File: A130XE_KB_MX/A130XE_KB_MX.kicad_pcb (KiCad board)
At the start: 2 copper layers, 330 x 131 mm, 76 parts, among them J1 34 pin RIBBON KEYBOARD CABLE, J2 Conn_01x02_Male, SW1 KS_RESET, SW10 K_5, SW11 K_I, SW12 K_T, SW13 K_G, SW14 K_SPACE, SW15 K_B, SW16 K_K, SW17 KS_SELECT, SW18 K_4, SW19 K_O, SW2 K_6, SW20 K_R, SW21 K_F, SW22 K_M, SW23 K_V, SW24 K_L, SW25 K_3, SW26 K_P, SW27 K_E, SW28 K_D, SW29 KS_START, SW3 K_U, SW30 K_comma, SW31 K_comdot, SW32 K_C, SW33 K_dot, SW34 K_2, SW35 K_minus, SW36 K_W, SW37 K_S, SW38 K_X, SW39 K_plus, SW4 K_Y, SW40 K_1, SW41 K_equal, SW42 K_Q, SW43 K_A, SW44 K_slash, SW45 K_asterisk, SW46 K_Z, SW47 K_ATARI, SW48 K_ESC, SW49 K_RETURN, SW5 K_H, SW50 K_TAB, SW51 K_CAPS, SW52 K_CTRL, SW53 K_LSHIFT, SW54 K_RSHIFT, SW55 K_BRK, SW56 K_DEL, SW57 K_GT, SW58 K_LT, SW59 K_0, SW6 K_N, SW60 K_9, SW61 K_8, SW62 K_7, SW63 K_SPACE_1, SW64 K_SPACE_2, SW65 K_F1, SW66 K_F2, SW67 K_F3, SW68 K_F4, SW7 KS_HELP, SW8 K_J, SW9 KS_OPTION

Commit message: New layout for spacebar 6.25 and two 1.25 at side. Function keys are 1.5u.
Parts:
- moved SW63 7.15 mm to (141.5, 198.1)
- moved SW64 2.41 mm to (284.3, 198.1)
- moved SW14 2.37 mm to (212.9, 198.1)
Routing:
- net OUT_7: track 413.6 -> 373.7 mm, vias 0 -> 1
- net IN_2: track 260.2 -> 297.0 mm
- net RSC: track 436.5 -> 402.2 mm, vias 2 -> 3
- net OUT_5: track 512.3 -> 480.4 mm, vias 1 -> 2
- net SELECT: track 178.8 -> 150.8 mm, vias 2 -> 0
- net GND: track 483.9 -> 457.2 mm, vias 0 -> 1
- net IN_5: track 304.5 -> 326.2 mm, vias 1 -> 0
- net IN_7: track 295.3 -> 316.0 mm, vias 2 -> 5
- net OPTION: track 124.9 -> 143.1 mm, vias 0 -> 1
- net START: track 163.6 -> 148.8 mm
- net IN_1: track 336.4 -> 325.1 mm, vias 1 -> 0
- net IN_6: track 314.3 -> 304.2 mm, vias 2 -> 0
- net IN_0: track 390.9 -> 400.5 mm, vias 4 -> 1
- net IN_4: track 356.1 -> 349.5 mm, vias 1 -> 0
- net OUT_4: track 287.7 -> 281.6 mm
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- added copper zone on B.Cu, net GND
- removed copper zone on B.Cu, net +5V

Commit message: Changed layout of buttons surrounding the spacebar. Atari XE seems to have 9U spacebar, so we are using 6.25u (more common) and two keys around it (1.25u and 1.50u)
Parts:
- SW63: footprint Button_Switch_Keyboard:SW_Cherry_MX1A_1.00u_PCB -> Button_Switch_Keyboard:SW_Cherry_MX1A_1.25u_PCB
- SW64: footprint Button_Switch_Keyboard:SW_Cherry_MX1A_1.00u_PCB -> Button_Switch_Keyboard:SW_Cherry_MX1A_1.50u_PCB
- moved SW64 2.41 mm to (286.8, 198.1)
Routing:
- net Net-(J2-Pad1): track 170.3 -> 174.8 mm, vias 0 -> 2
- net GND: track 457.2 -> 461.5 mm
- net IN_6: track 304.2 -> 302.9 mm, vias 0 -> 1

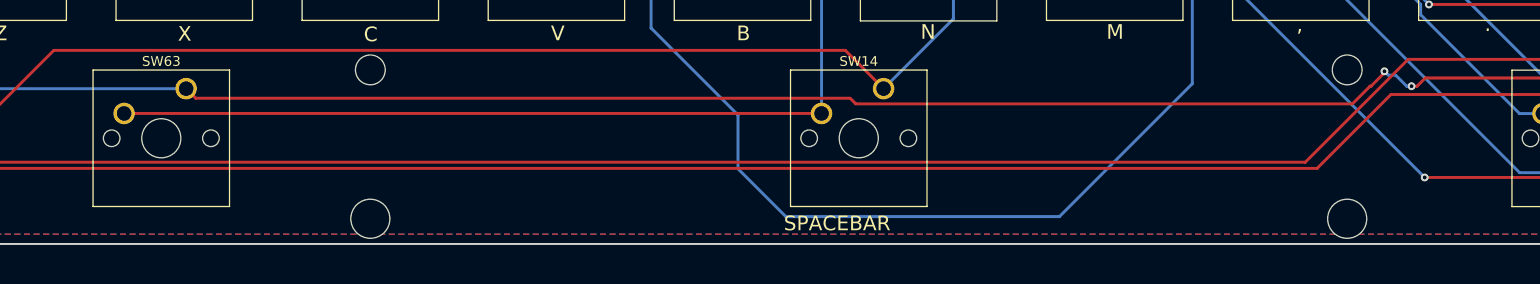
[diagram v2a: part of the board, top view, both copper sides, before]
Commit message: Added silkscreen print for spacebar sizes
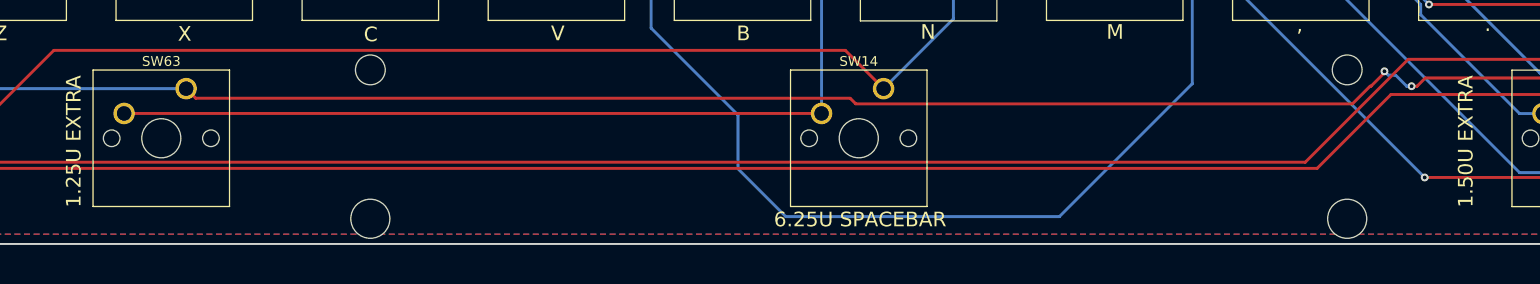
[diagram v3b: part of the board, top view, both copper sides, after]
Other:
- board text added: "1.25U EXTRA"
- board text added: "1.50U EXTRA"
- board text added: "6.25U SPACEBAR"
- board text removed: "SPACEBAR"
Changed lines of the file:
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@@
   (general
     (thickness 1.6)
-    (drawings 714)
+    (drawings 716)
     (tracks 594)
     (zones 0)
@@
     )
   )
+  (gr_text "1.50U EXTRA" (at 272.5 203.5 90) (layer F.SilkS)
+    (effects (font (size 1.5 1.5) (thickness 0.3)))
+  )
+  (gr_text "1.25U EXTRA" (at 130 203.5 90) (layer F.SilkS)
+    (effects (font (size 1.5 1.5) (thickness 0.3)))
+  )
   (gr_line (start 234.3 139.074593) (end 248.299 139.074593) (layer Cmts.User) (width 0.2))
   (gr_line (start 253.35 153.073893) (end 253.35 139.074593) (layer Cmts.User) (width 0.2))
@@
     (effects (font (size 1.5 1.5) (thickness 0.3)) (justify mirror))
   )
-  (gr_text SPACEBAR (at 208.15 211.9) (layer F.SilkS)
+  (gr_text "6.25U SPACEBAR" (at 210.5 211.5) (layer F.SilkS)
     (effects (font (size 1.5 1.5) (thickness 0.3)))
   )
@@
     (arrow2b (pts (xy 47 72) (xy 48.126504 71.413579)))
   )
+  (segment (start 285.1748 203.2705) (end 285.1748 203.0166) (width 0.3) (layer F.Cu) (net 0))
   (segment (start 296.7777 197.0219) (end 294.1352 199.6644) (width 0.3) (layer B.Cu) (net 1))
   (segment (start 301.14 199.6997) (end 298.4622 197.0219) (width 0.3) (layer B.Cu) (net 1))
@@
   (segment (start 258.65 92.54) (end 287.65 92.54) (width 0.3) (layer F.Cu) (net 1))
   (via (at 294.1352 199.6644) (size 0.8) (layers F.Cu B.Cu) (net 1))
-  (segment (start 285.1748 203.2705) (end 285.1748 203.0166) (width 0.3) (layer F.Cu) (net 0))
   (segment (start 256.0693 205.6303) (end 266.5996 195.1) (width 0.3) (layer F.Cu) (net 1))
   (segment (start 52.775 210.75) (end 57.8947 205.6303) (width 0.3) (layer F.Cu) (net 1))

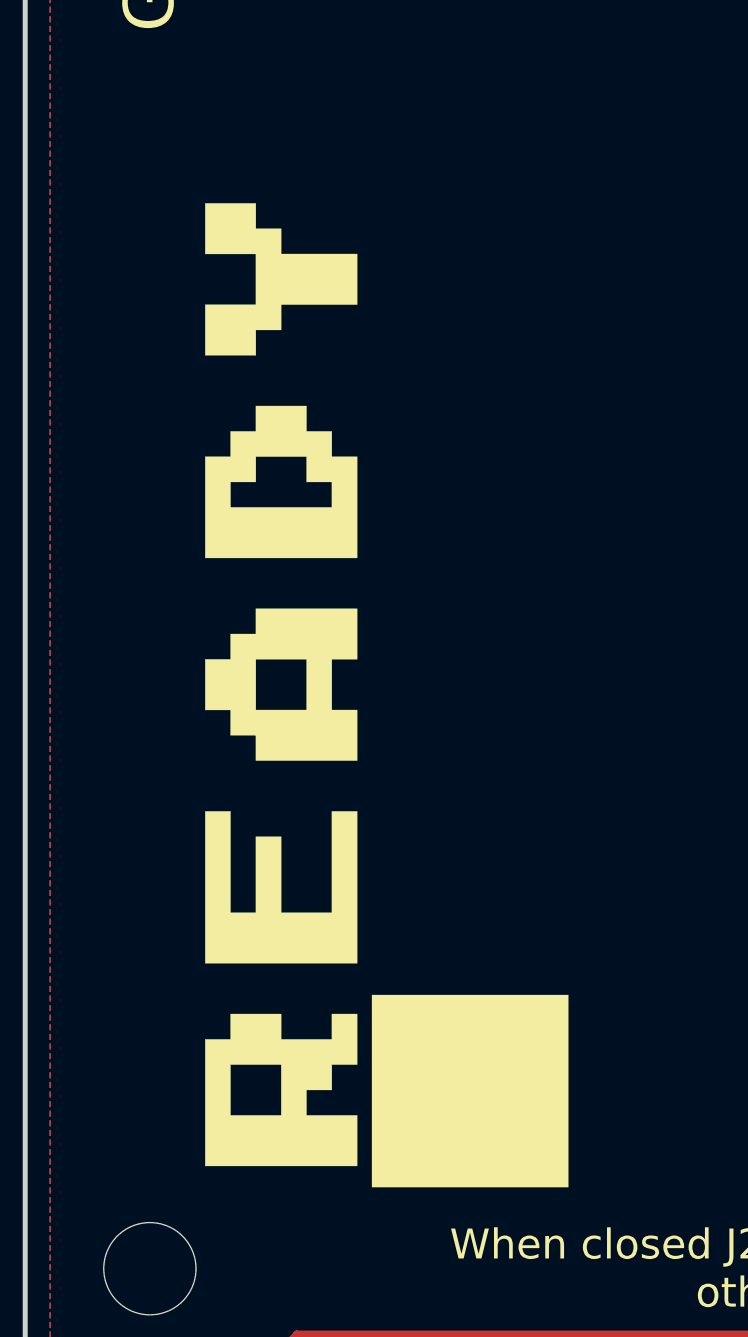
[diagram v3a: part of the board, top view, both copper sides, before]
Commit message: Added new footprints for keys (with 3D WRL and Stabilizers where needed)
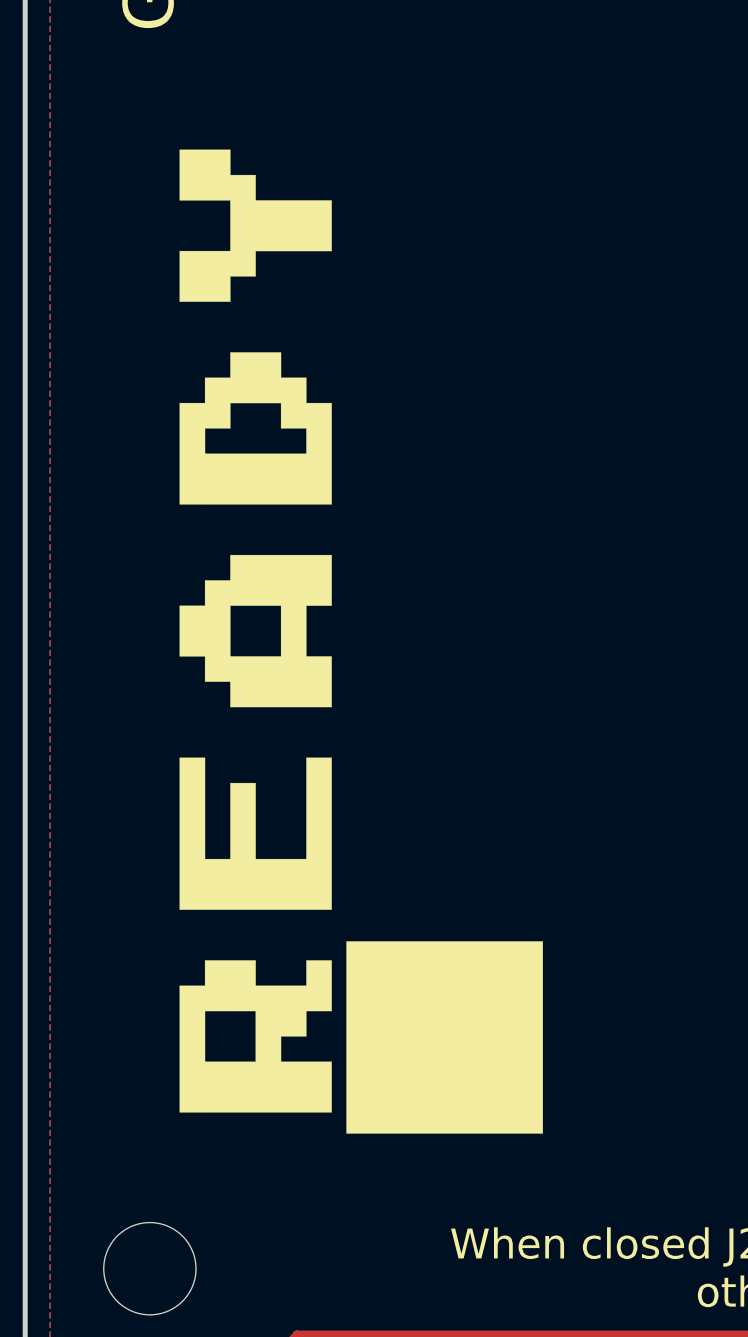
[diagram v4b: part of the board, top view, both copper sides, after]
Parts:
- SW1, SW17, SW29, SW7, SW9: footprint Button_Switch_Keyboard:SW_Cherry_MX1A_1.00u_PCB -> RetroBitLab:SW_Cherry_MX1A_1.50u_PCB_3d
- SW10, SW11, SW12, SW13, SW15, SW16, SW18, SW19, SW2, SW20, SW21, SW22, SW23, SW24, SW25, SW26, SW27, SW28, SW3, SW30, SW31, SW32, SW33, SW34, SW35, SW36, SW37, SW38, SW39, SW4, SW40, SW41, SW42, SW43, SW44, SW45, SW46, SW47, SW48, SW5, SW55, SW56, SW57, SW58, SW59, SW6, SW60, SW61, SW62, SW65, SW66, SW67, SW68, SW8: footprint Button_Switch_Keyboard:SW_Cherry_MX1A_1.00u_PCB -> RetroBitLab:SW_Cherry_MX1A_1.00u_PCB_3d
- SW14: footprint Button_Switch_Keyboard:SW_Cherry_MX1A_6.25u_PCB -> RetroBitLab:SW_Cherry_MX1A_6.25u_PCB_3d
- SW49, SW50, SW64: footprint Button_Switch_Keyboard:SW_Cherry_MX1A_1.50u_PCB -> RetroBitLab:SW_Cherry_MX1A_1.50u_PCB_3d
- SW51, SW63: footprint Button_Switch_Keyboard:SW_Cherry_MX1A_1.25u_PCB -> RetroBitLab:SW_Cherry_MX1A_1.25u_PCB_3d
- SW52, SW54: footprint Button_Switch_Keyboard:SW_Cherry_MX1A_1.75u_PCB -> RetroBitLab:SW_Cherry_MX1A_1.75u_PCB_3d
- SW53: footprint Button_Switch_Keyboard:SW_Cherry_MX1A_2.25u_PCB -> RetroBitLab:SW_Cherry_MX1A_2.25u_PCB_3d
- moved G*** 2.38 mm to (60.5, 177.9)
